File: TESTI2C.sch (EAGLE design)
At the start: 20 parts, among them J1 Digital_0_7, J2 Analog, J3 Digital_8_13

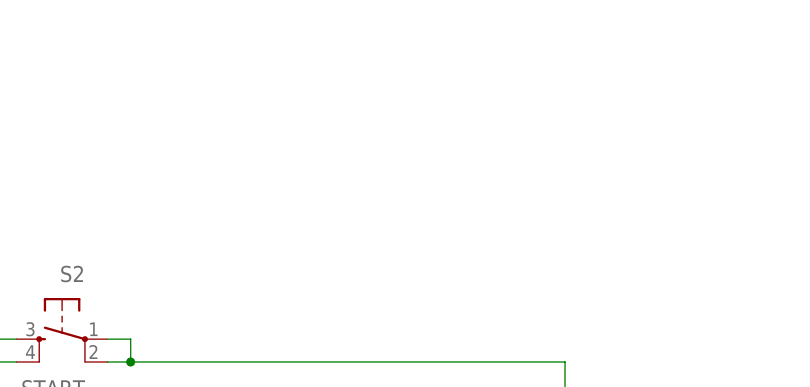
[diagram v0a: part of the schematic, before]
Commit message: Added piezo
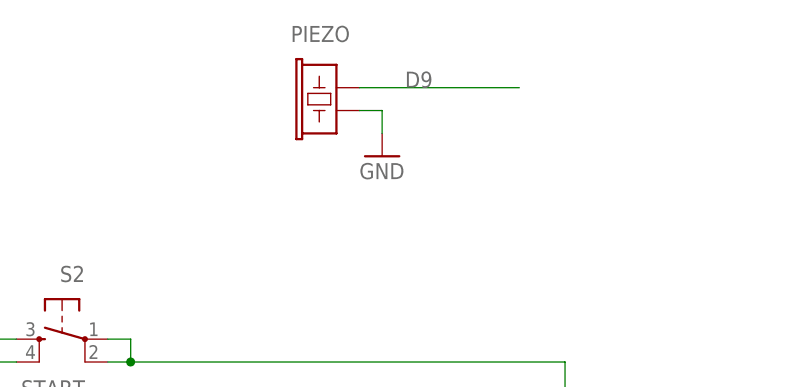
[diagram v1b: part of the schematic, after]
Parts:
- added PIEZO: BUZZERSMD12X12, freetronics-master-v1:BUZZERSMD12X12
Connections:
- net D9: now also PIEZO.2
- net GND: now also PIEZO.1
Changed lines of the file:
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@@
 <part name="LED4" library="freetronics-jon" deviceset="LED" device="0603" value="BLUE"/>
 <part name="R5" library="freetronics-jon" deviceset="RESISTOR" device="0603" value="1K5 0603"/>
+<part name="PIEZO" library="freetronics-master-v1" deviceset="BUZZER" device="SMD12X12"/>
+<part name="GND3" library="SparkFun" deviceset="GND" device=""/>
 </parts>
 <sheets>
@@
 <instance part="LED4" gate="G$1" x="43.18" y="142.24"/>
 <instance part="R5" gate="G$1" x="43.18" y="121.92" rot="R90"/>
+<instance part="PIEZO" gate="G$1" x="160.02" y="157.48" smashed="yes" rot="R90">
+<attribute name="NAME" x="154.94" y="165.1" size="1.778" layer="95"/>
+</instance>
+<instance part="GND3" gate="1" x="165.1" y="152.4"/>
 </instances>
 <busses>
@@
 <junction x="127" y="35.56"/>
 </segment>
+<segment>
+<wire x1="165.1" y1="154.94" x2="165.1" y2="157.48" width="0.1524" layer="91"/>
+<wire x1="165.1" y1="157.48" x2="162.56" y2="157.48" width="0.1524" layer="91"/>
+<pinref part="PIEZO" gate="G$1" pin="1"/>
+<pinref part="GND3" gate="1" pin="GND"/>
+</segment>
 </net>
 <net name="VIN" class="0">
@@
 <pinref part="J3" gate="G$1" pin="2"/>
 </segment>
-</net>
+<segment>
+<wire x1="180.34" y1="160.02" x2="162.56" y2="160.02" width="0.1524" layer="91"/>
+<pinref part="PIEZO" gate="G$1" pin="2"/>
+<label x="167.64" y="160.02" size="1.778" layer="95"/>
+</segment>
+</net>

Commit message: Routing and silkscreen for v1.0 release
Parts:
- R1, R2, R3: value 560R 0603 -> 560R
- R4: value 1K 0603 -> 1K
- R5: value 1K5 0603 -> 1K5
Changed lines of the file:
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@@
 <part name="LED2" library="freetronics-jon" deviceset="LED" device="0603" value="YELLOW TEST"/>
 <part name="LED3" library="freetronics-jon" deviceset="LED" device="0603" value="RED FAIL"/>
-<part name="R1" library="freetronics-jon" deviceset="RESISTOR" device="0603" value="560R 0603"/>
-<part name="R2" library="freetronics-jon" deviceset="RESISTOR" device="0603" value="560R 0603"/>
-<part name="R3" library="freetronics-jon" deviceset="RESISTOR" device="0603" value="560R 0603"/>
+<part name="R1" library="freetronics-jon" deviceset="RESISTOR" device="0603" value="560R"/>
+<part name="R2" library="freetronics-jon" deviceset="RESISTOR" device="0603" value="560R"/>
+<part name="R3" library="freetronics-jon" deviceset="RESISTOR" device="0603" value="560R"/>
 <part name="GND2" library="freetronics" deviceset="GND" device=""/>
 <part name="S2" library="freetronics" deviceset="TAC_SWITCH" device="PTH" value="START"/>
-<part name="R4" library="freetronics-jon" deviceset="RESISTOR" device="0603" value="1K 0603"/>
+<part name="R4" library="freetronics-jon" deviceset="RESISTOR" device="0603" value="1K"/>
 <part name="JP1" library="freetronics-master-v1.1" deviceset="M04" device="PTH" value="MODULE"/>
 <part name="LED4" library="freetronics-jon" deviceset="LED" device="0603" value="BLUE"/>
-<part name="R5" library="freetronics-jon" deviceset="RESISTOR" device="0603" value="1K5 0603"/>
+<part name="R5" library="freetronics-jon" deviceset="RESISTOR" device="0603" value="1K5"/>
 <part name="PIEZO" library="freetronics-master-v1" deviceset="BUZZER" device="SMD12X12"/>
 <part name="GND3" library="SparkFun" deviceset="GND" device=""/>
